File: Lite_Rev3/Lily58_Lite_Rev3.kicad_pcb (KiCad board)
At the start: 2 copper layers, 218.5 x 159.5 mm, 118 parts, among them J1 M2HOLE, J10 M2HOLE, J11 M2HOLE, J12 HOLE, J13 HOLE, J14 HOLE, J15 HOLE, J16 OLED_R, J17 breakaway, J18 breakaway, J19 breakaway, J2 M2HOLE, J20 breakaway, J21 breakaway, J22 AudioJack4, J23 HOLE, J24 HOLE, J25 breakaway, J26 breakaway, J3 HOLE, J4 HOLE, J5 HOLE, J6 HOLE, J7 OLED_L, J8 breakaway, J9 AudioJack4, SW1 SW_Push, SW10 SW_Push, SW11 SW_Push, SW12 SW_Push, SW13 SW_Push, SW14 SW_Push, SW15 SW_Push, SW16 SW_Push, SW17 SW_Push, SW18 SW_Push, SW19 SW_Push, SW2 SW_Push, SW20 SW_Push, SW21 SW_Push, SW22 SW_Push, SW23 SW_Push, SW24 SW_Push, SW25 SW_Push, SW26 SW_Push, SW27 SW_Push, SW28 SW_Push, SW29 SW_Push, SW3 SW_Push, SW30 SW_Push, SW31 SW_Push, SW32 SW_Push, SW33 SW_Push, SW34 SW_Push, SW35 SW_Push, SW36 SW_Push, SW37 SW_Push, SW38 SW_Push, SW39 SW_Push, SW4 SW_Push, SW40 SW_Push, SW41 SW_Push, SW42 SW_Push, SW43 SW_Push, SW44 SW_Push, SW45 SW_Push, SW46 SW_Push, SW47 SW_Push, SW48 SW_Push, SW49 SW_Push, SW5 SW_Push, SW50 SW_Push, SW51 SW_Push, SW52 SW_Push, SW53 SW_Push, SW54 SW_Push, SW55 SW_Push, SW56 SW_Push, SW57 SW_Push, SW58 SW_Push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

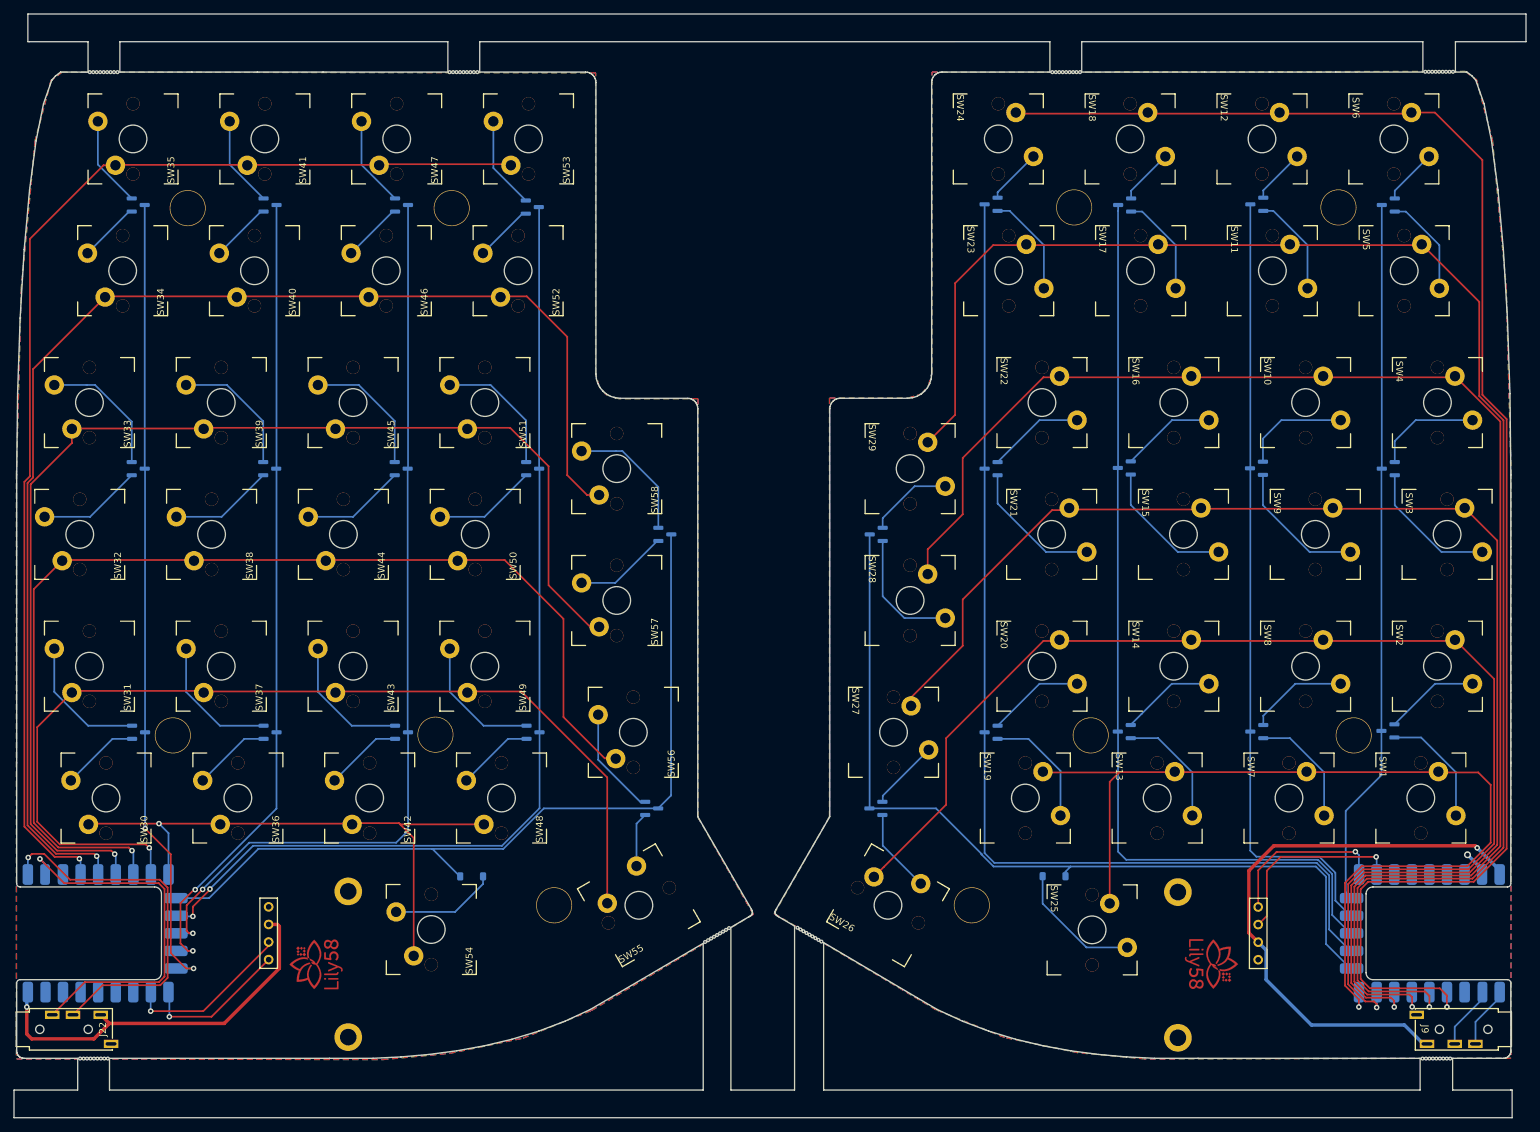
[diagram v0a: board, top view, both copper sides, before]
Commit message: [Lily58 Lite Rev3] fix cols pin
Changed to the same cols pin as Lily58 Pro and Lily58 Pro v2
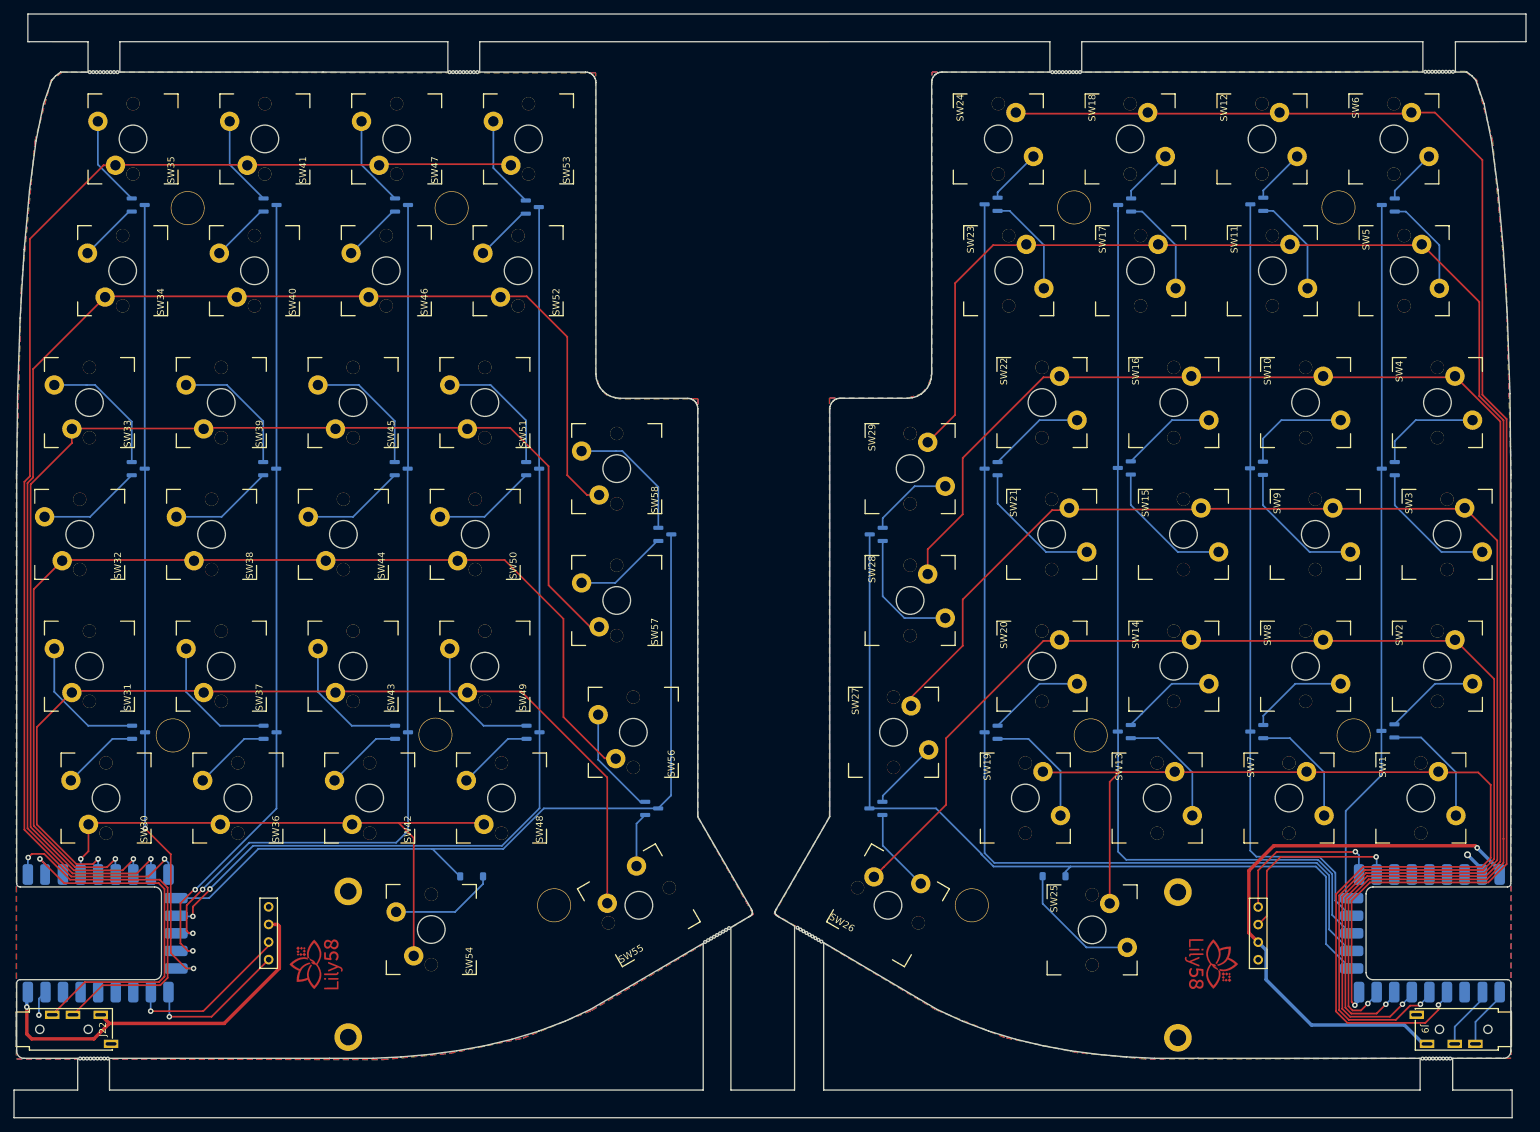
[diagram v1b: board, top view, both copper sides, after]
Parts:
- J12, J13, J14, J15, J23, J24, J3, J4, J5, J6: footprint yuchi:HOLE_M2_TH_5mm -> yuchi:HOLE_M2_TH
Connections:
- SW1 pad 1: COL0_L -> COL5_L
- SW10 pad 1: COL3_L -> COL2_L
- SW11 pad 1: COL4_L -> COL1_L
- SW12 pad 1: COL5_L -> COL0_L
- SW13 pad 1: COL0_L -> COL5_L
- SW14 pad 1: COL1_L -> COL4_L
- SW15 pad 1: COL2_L -> COL3_L
- SW16 pad 1: COL3_L -> COL2_L
- SW17 pad 1: COL4_L -> COL1_L
- SW18 pad 1: COL5_L -> COL0_L
- SW19 pad 1: COL0_L -> COL5_L
- SW2 pad 1: COL1_L -> COL4_L
- SW20 pad 1: COL1_L -> COL4_L
- SW21 pad 1: COL2_L -> COL3_L
- SW22 pad 1: COL3_L -> COL2_L
- SW23 pad 1: COL4_L -> COL1_L
- SW24 pad 1: COL5_L -> COL0_L
- SW25 pad 1: COL0_L -> COL5_L
- SW26 pad 1: COL1_L -> COL4_L
- SW27 pad 1: COL2_L -> COL3_L
- SW28 pad 1: COL3_L -> COL2_L
- SW29 pad 1: COL4_L -> COL1_L
- SW3 pad 1: COL2_L -> COL3_L
- SW30 pad 1: COL0_R -> COL5_R
- SW31 pad 1: COL1_R -> COL4_R
- SW32 pad 1: COL2_R -> COL3_R
- SW33 pad 1: COL3_R -> COL2_R
- SW34 pad 1: COL4_R -> COL1_R
- SW35 pad 1: COL5_R -> COL0_R
- SW36 pad 1: COL0_R -> COL5_R
- SW37 pad 1: COL1_R -> COL4_R
- SW38 pad 1: COL2_R -> COL3_R
- SW39 pad 1: COL3_R -> COL2_R
- SW4 pad 1: COL3_L -> COL2_L
- SW40 pad 1: COL4_R -> COL1_R
- SW41 pad 1: COL5_R -> COL0_R
- SW42 pad 1: COL0_R -> COL5_R
- SW43 pad 1: COL1_R -> COL4_R
- SW44 pad 1: COL2_R -> COL3_R
- SW45 pad 1: COL3_R -> COL2_R
- SW46 pad 1: COL4_R -> COL1_R
- SW47 pad 1: COL5_R -> COL0_R
- SW48 pad 1: COL0_R -> COL5_R
- SW49 pad 1: COL1_R -> COL4_R
- SW5 pad 1: COL4_L -> COL1_L
- SW50 pad 1: COL2_R -> COL3_R
- SW51 pad 1: COL3_R -> COL2_R
- SW52 pad 1: COL4_R -> COL1_R
- SW53 pad 1: COL5_R -> COL0_R
- SW54 pad 1: COL0_R -> COL5_R
- SW55 pad 1: COL1_R -> COL4_R
- SW56 pad 1: COL2_R -> COL3_R
- SW57 pad 1: COL3_R -> COL2_R
- SW58 pad 1: COL4_R -> COL1_R
- SW6 pad 1: COL5_L -> COL0_L
- SW7 pad 1: COL0_L -> COL5_L
- SW8 pad 1: COL1_L -> COL4_L
- SW9 pad 1: COL2_L -> COL3_L
- U1 pad 26: RESET_L -> unconnected-(U1-GP26-Pad26)
- U2 pad 26: RESET_R -> unconnected-(U2-GP26-Pad26)
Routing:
- net COL0_R: track 85.4 -> 186.6 mm
- net COL5_R: track 171.6 -> 85.6 mm
- net COL0_L: track 138.1 -> 215.9 mm
- net COL5_L: track 225.4 -> 156.7 mm
- net COL1_R: track 143.7 -> 200.5 mm
- net COL4_R: track 190.9 -> 136.2 mm
- net COL1_L: track 182.0 -> 234.6 mm
- net COL4_L: track 238.7 -> 194.9 mm
- net COL2_L: track 195.4 -> 217.6 mm
- net COL2_R: track 159.5 -> 179.0 mm
- net COL3_R: track 175.1 -> 157.6 mm
- net COL3_L: track 216.0 -> 202.7 mm
- net GNDA: track 0.00 -> 3.72 mm, vias 0 -> 1
- net Net-(D3-A-Pad1): track 9.41 -> 8.11 mm
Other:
- outline, holes or cut-outs redrawn
- board text added: "2024-08-13"
- board text added: "Lily58 Lite Rev3 v4 PCBA"
- board text added: "PCB Design by yuchi(Liliums)"
- board text added: "PCB-L"
- board text added: "PCB-R"
- board text removed: "2024-07-18"
- board text removed: "Lily58 Lite Rev3 v3 PCBA"
- board text removed: "PCB Design by yuchi"

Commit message: [Lily58 Lite Rev3] Fix SW54
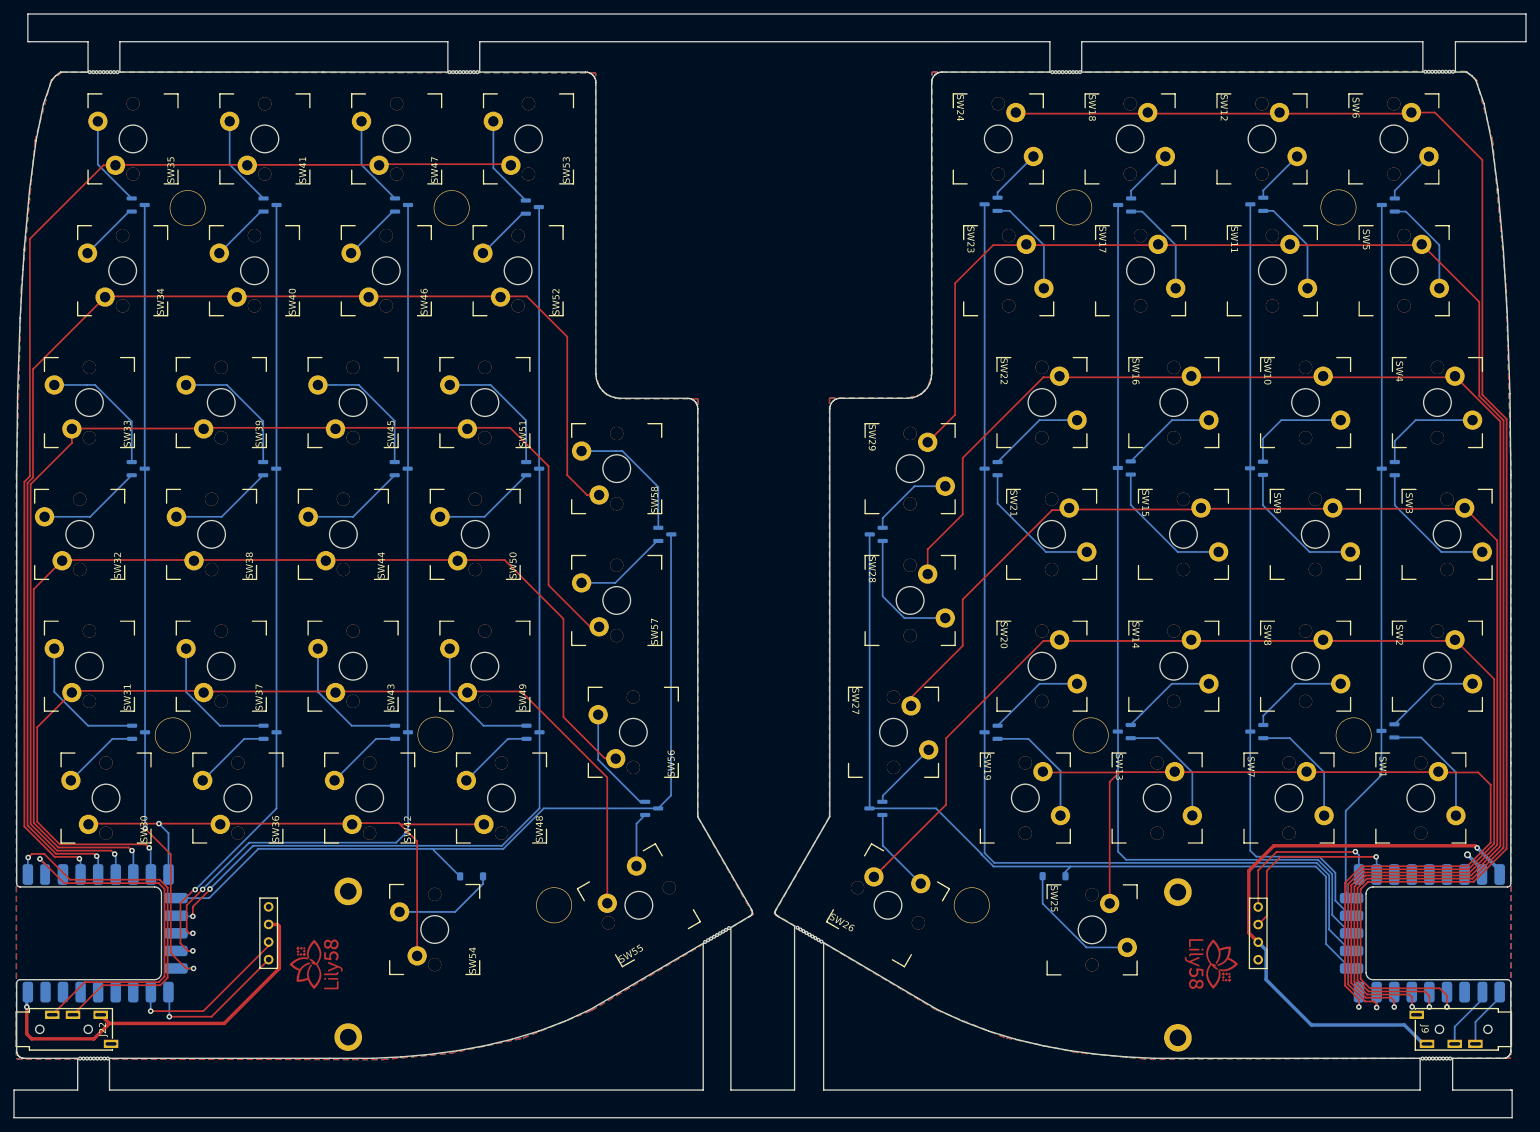
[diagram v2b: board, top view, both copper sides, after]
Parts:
- J12, J13, J14, J15, J23, J24, J3, J4, J5, J6: footprint yuchi:HOLE_M2_TH -> yuchi:HOLE_M2_TH_5mm
- moved SW54 0.50 mm to (165.2, 183.2)
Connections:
- SW1 pad 1: COL5_L -> COL0_L
- SW10 pad 1: COL2_L -> COL3_L
- SW11 pad 1: COL1_L -> COL4_L
- SW12 pad 1: COL0_L -> COL5_L
- SW13 pad 1: COL5_L -> COL0_L
- SW14 pad 1: COL4_L -> COL1_L
- SW15 pad 1: COL3_L -> COL2_L
- SW16 pad 1: COL2_L -> COL3_L
- SW17 pad 1: COL1_L -> COL4_L
- SW18 pad 1: COL0_L -> COL5_L
- SW19 pad 1: COL5_L -> COL0_L
- SW2 pad 1: COL4_L -> COL1_L
- SW20 pad 1: COL4_L -> COL1_L
- SW21 pad 1: COL3_L -> COL2_L
- SW22 pad 1: COL2_L -> COL3_L
- SW23 pad 1: COL1_L -> COL4_L
- SW24 pad 1: COL0_L -> COL5_L
- SW25 pad 1: COL5_L -> COL0_L
- SW26 pad 1: COL4_L -> COL1_L
- SW27 pad 1: COL3_L -> COL2_L
- SW28 pad 1: COL2_L -> COL3_L
- SW29 pad 1: COL1_L -> COL4_L
- SW3 pad 1: COL3_L -> COL2_L
- SW30 pad 1: COL5_R -> COL0_R
- SW31 pad 1: COL4_R -> COL1_R
- SW32 pad 1: COL3_R -> COL2_R
- SW33 pad 1: COL2_R -> COL3_R
- SW34 pad 1: COL1_R -> COL4_R
- SW35 pad 1: COL0_R -> COL5_R
- SW36 pad 1: COL5_R -> COL0_R
- SW37 pad 1: COL4_R -> COL1_R
- SW38 pad 1: COL3_R -> COL2_R
- SW39 pad 1: COL2_R -> COL3_R
- SW4 pad 1: COL2_L -> COL3_L
- SW40 pad 1: COL1_R -> COL4_R
- SW41 pad 1: COL0_R -> COL5_R
- SW42 pad 1: COL5_R -> COL0_R
- SW43 pad 1: COL4_R -> COL1_R
- SW44 pad 1: COL3_R -> COL2_R
- SW45 pad 1: COL2_R -> COL3_R
- SW46 pad 1: COL1_R -> COL4_R
- SW47 pad 1: COL0_R -> COL5_R
- SW48 pad 1: COL5_R -> COL0_R
- SW49 pad 1: COL4_R -> COL1_R
- SW5 pad 1: COL1_L -> COL4_L
- SW50 pad 1: COL3_R -> COL2_R
- SW51 pad 1: COL2_R -> COL3_R
- SW52 pad 1: COL1_R -> COL4_R
- SW53 pad 1: COL0_R -> COL5_R
- SW54 pad 1: COL5_R -> COL0_R
- SW55 pad 1: COL4_R -> COL1_R
- SW56 pad 1: COL3_R -> COL2_R
- SW57 pad 1: COL2_R -> COL3_R
- SW58 pad 1: COL1_R -> COL4_R
- SW6 pad 1: COL0_L -> COL5_L
- SW7 pad 1: COL5_L -> COL0_L
- SW8 pad 1: COL4_L -> COL1_L
- SW9 pad 1: COL3_L -> COL2_L
- U1 pad 26: unconnected-(U1-GP26-Pad26) -> RESET_L
- U2 pad 26: unconnected-(U2-GP26-Pad26) -> RESET_R
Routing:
- net COL0_R: track 186.6 -> 85.6 mm
- net COL5_R: track 85.6 -> 171.6 mm
- net COL0_L: track 215.9 -> 138.1 mm
- net COL5_L: track 156.7 -> 225.4 mm
- net COL1_R: track 200.5 -> 143.7 mm
- net COL4_R: track 136.2 -> 190.9 mm
- net COL1_L: track 234.6 -> 182.0 mm
- net COL4_L: track 194.9 -> 238.7 mm
- net COL2_L: track 217.6 -> 195.4 mm
- net COL2_R: track 179.0 -> 159.5 mm
- net COL3_R: track 157.6 -> 175.1 mm
- net COL3_L: track 202.7 -> 216.0 mm
- net GNDA: track 3.72 -> 0.00 mm, vias 1 -> 0
- net Net-(D3-A-Pad1): track 8.11 -> 9.41 mm
- net Net-(D30-A): track 15.3 -> 14.8 mm
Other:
- outline, holes or cut-outs redrawn
- board text added: "2024-10-15"
- board text added: "Lily58 Lite Rev3 v3 PCBA"
- board text added: "PCB Design by yuchi"
- board text removed: "2024-08-13"
- board text removed: "Lily58 Lite Rev3 v4 PCBA"
- board text removed: "PCB Design by yuchi(Liliums)"
- board text removed: "PCB-L"
- board text removed: "PCB-R"
